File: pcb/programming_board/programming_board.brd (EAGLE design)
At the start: 100 x 80 mm, 28 parts, among them IC1 4053D, IC2 74ABT125PW

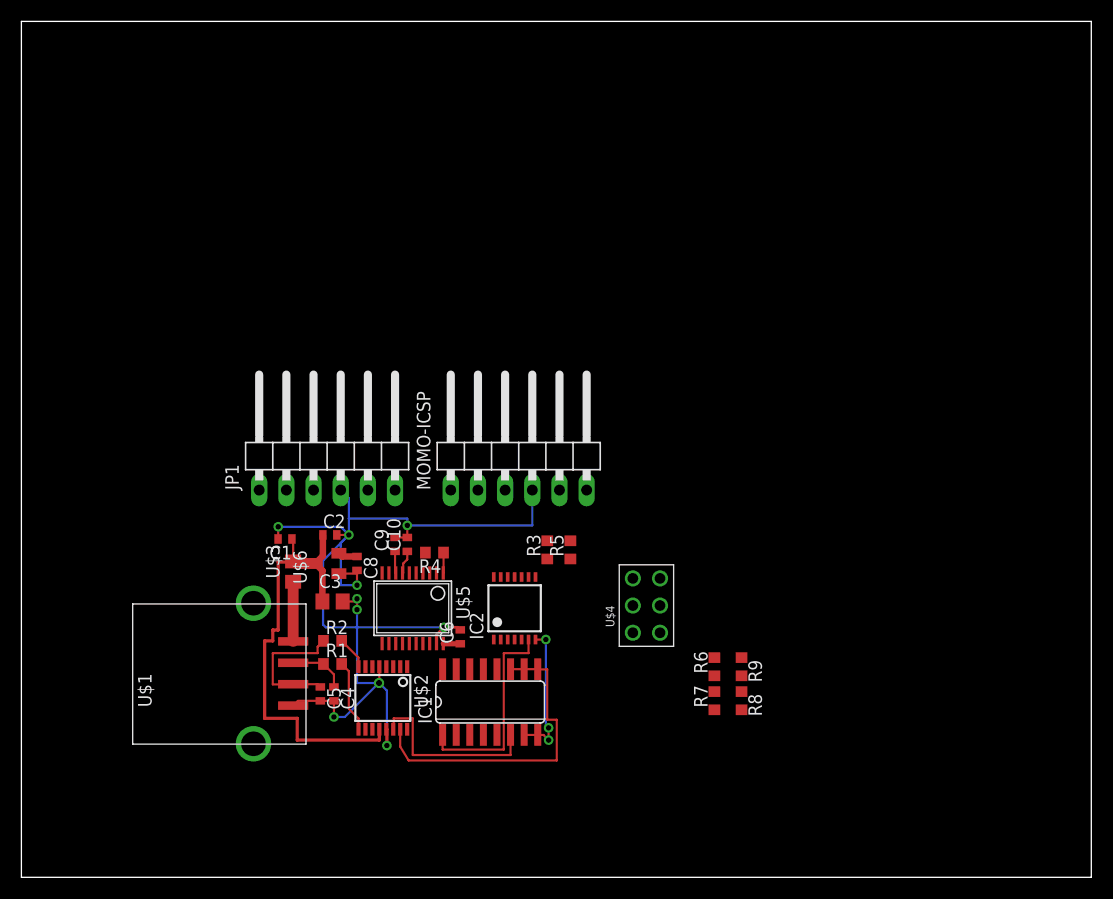
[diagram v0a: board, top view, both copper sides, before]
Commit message: Laid out first complete version of pcb
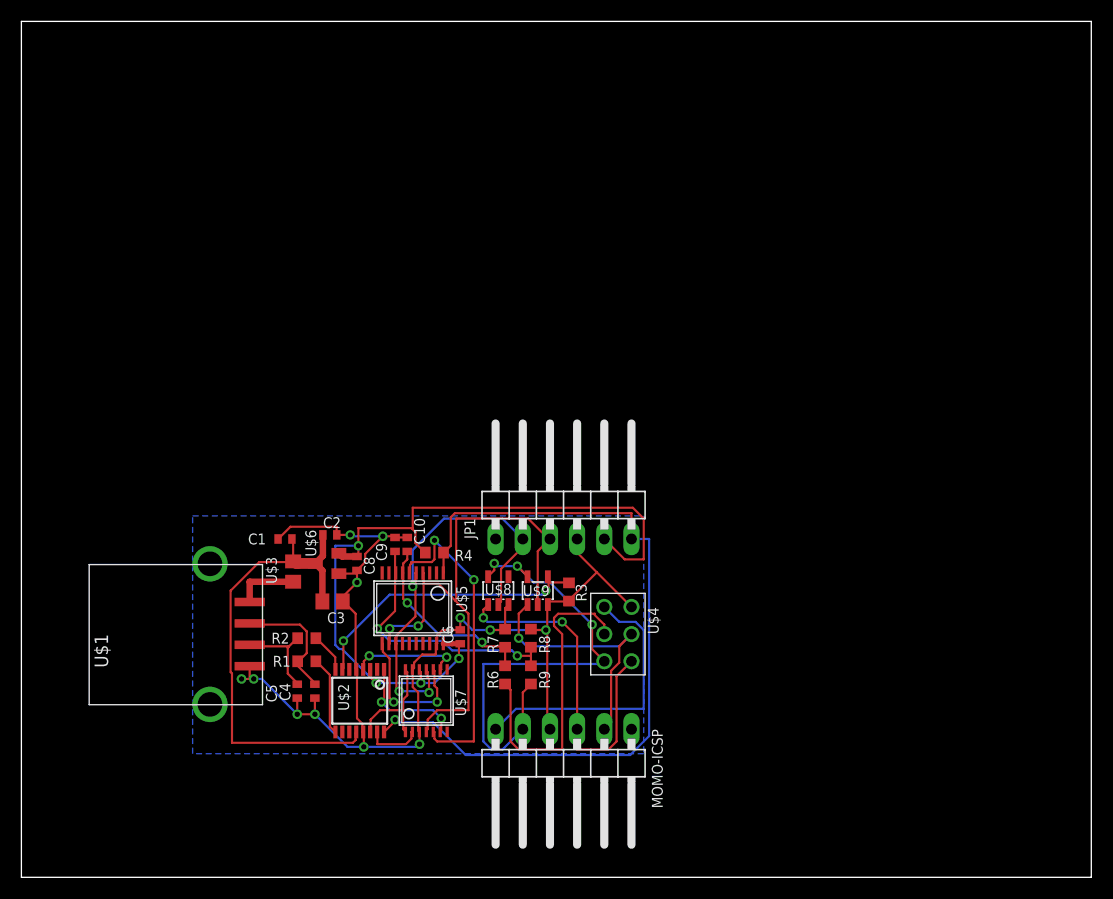
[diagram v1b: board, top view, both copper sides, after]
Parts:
- removed IC1: 4053D, 40xx:SO16
- removed IC2: 74ABT125PW, 74xx-us:TSSOP14
- removed R5: (no value), rcl:R0603
- added U$7: DG636, components:TSSOP14
- added U$8, U$9: TS5A1066-SPST, components:SOT23-5L
- R4: value (none) -> 10K
- moved MOMO-ICSP 30.3 mm to (50.7, 10.0), turned to 180 degrees
- moved JP1 22.6 mm to (50.7, 35.4)
- moved R8 20.5 mm to (47.6, 22.4)
- moved R7 20.4 mm to (45.2, 22.4), turned to 270 degrees
- moved R9 19.7 mm to (47.6, 18.9)
- moved R6 19.6 mm to (45.2, 18.9), turned to 270 degrees
- moved U$1 5.48 mm to (21.3, 22.7)
- moved R3 4.43 mm to (51.2, 26.7)
- moved U$4 2.67 mm to (57.0, 22.7), turned to 90 degrees
- moved R1 2.43 mm to (26.7, 20.2)
- moved R2 2.43 mm to (26.7, 22.4)
- moved C5 2.17 mm to (25.8, 17.4)
- moved U$2 2.17 mm to (31.6, 16.5)
- moved C4 1.80 mm to (27.4, 17.4)
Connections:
- removed net N$12: IC1.1, IC2.6
- removed net N$13: IC1.3, IC2.2
- removed net N$14: IC2.9, U$5.11
- removed net N$15: IC2.11, U$5.6
- removed net N$16: IC2.10, IC2.13, R5.1, U$5.13
- removed net N$18: IC1.5, JP1.2, U$5.5
- removed net N$19: IC1.2, JP1.3, U$5.4
- removed net N$8: IC1.15, U$2.4
- removed net N$9: IC1.10, IC1.11, IC1.9, U$2.15
- new net CLOCKRX: JP1.3, U$5.12, U$5.4, U$7.4, U$9.2
- new net DATATX: JP1.2, U$5.13, U$5.5, U$7.11, U$8.2
- new net PICRX1: U$5.6, U$7.5
- new net PICTX1: U$5.11, U$7.10
- new net USBRX: U$2.4, U$7.9
- new net USBTX: U$2.1, U$7.6
- net +3V3: now also U$8.5, U$9.5; no longer IC2.14, R3.2, R5.2
- net GND: now also R3.1, U$7.13, U$7.3, U$8.3, U$9.3; no longer IC1.7, IC1.8, IC2.7
- net N$10: now also U$2.15, U$7.2; no longer IC2.1, IC2.4, R3.1, U$2.7
- net N$11: now also U$7.1, U$7.14; no longer IC1.6
- net N$21: now also U$2.16
- net N$7: now also R3.2, U$2.7, U$9.4; no longer IC1.4, U$2.1
- net PGC: now also U$9.1; no longer IC2.3, IC2.8
- net PGD: now also U$8.1; no longer IC2.12, IC2.5
- net VCCIO: now also U$7.12; no longer IC1.16
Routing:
- net VCCIO: track 3.41 -> 76.0 mm, vias 0 -> 4
- net N$21: track 1.92 -> 72.5 mm, vias 0 -> 1
- net CLOCKRX: track 0.00 -> 53.1 mm, vias 0 -> 2
- net +3V3: track 0.00 -> 46.2 mm, vias 0 -> 3
- net DATATX: track 0.00 -> 40.2 mm, vias 0 -> 3
- net PGD: track 0.00 -> 33.5 mm, vias 0 -> 2
- net PICRX1: track 0.00 -> 30.0 mm, vias 0 -> 2
- net N$9: track 29.8 -> 0.00 mm
- net V+: track 0.00 -> 29.6 mm
- net N$7: track 0.00 -> 27.5 mm, vias 0 -> 2
- net N$6: track 0.00 -> 26.6 mm
- net PGC: track 0.00 -> 24.8 mm, vias 0 -> 1
- net N$20: track 2.08 -> 25.1 mm, vias 0 -> 2
- net N$12: track 19.7 -> 0.00 mm
- net N$17: track 2.24 -> 18.1 mm, vias 0 -> 2
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- added copper zone on layer 16, net GND

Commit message: Finished programming board (Momo Field Service Unit)
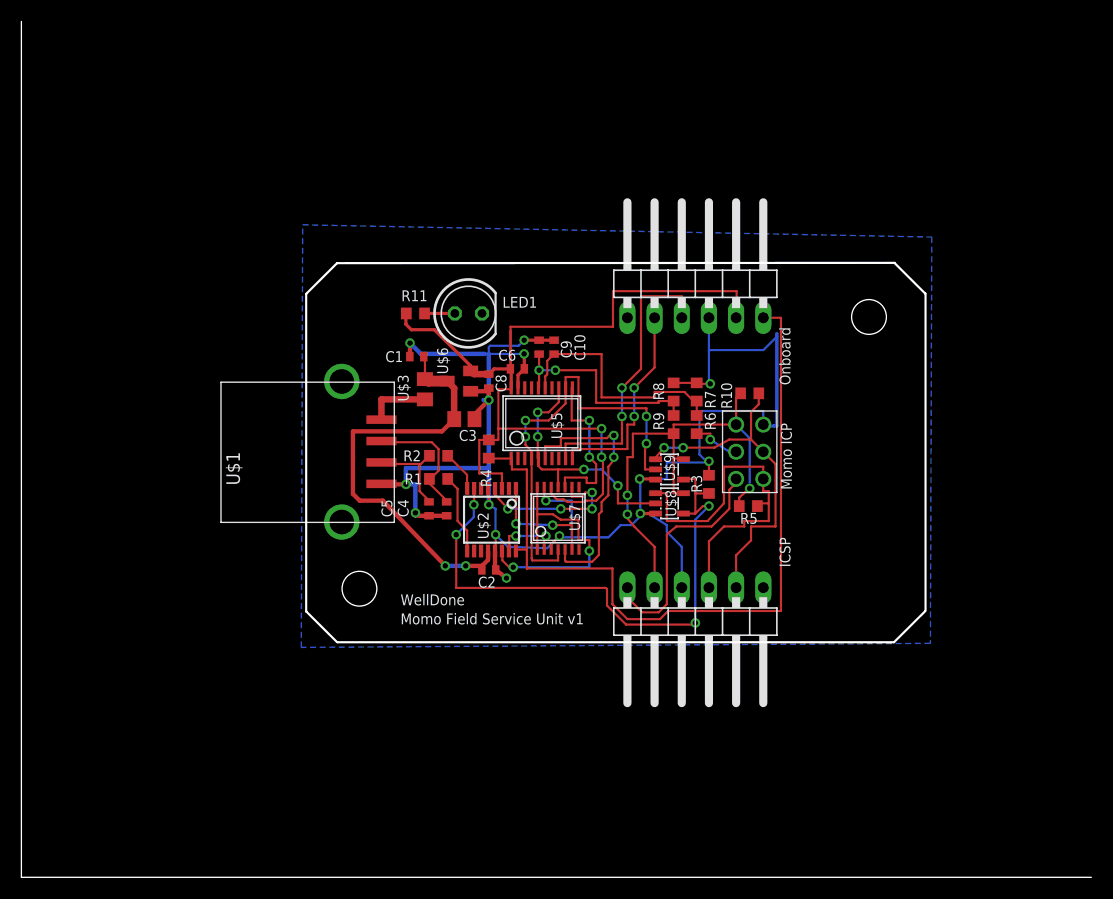
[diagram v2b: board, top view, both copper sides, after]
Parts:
- added LED1: (no value), led:LED5MM
- added R10: 10K, rcl:R0603
- added R11: 66R, rcl:R0603
- added R5: 19K, rcl:R0603
- moved R6 29.5 mm to (63.1, 42.3)
- moved R7 29.2 mm to (63.1, 45.4)
- moved R9 26.9 mm to (61.0, 42.3)
- moved R8 26.6 mm to (61.0, 45.4)
- moved C6 25.6 mm to (46.4, 47.5), turned to 0 degrees
- moved JP1 24.1 mm to (63.0, 56.1)
- moved C10 23.0 mm to (49.8, 49.6)
- moved C9 22.8 mm to (48.4, 49.6)
- moved U$5 21.1 mm to (48.6, 42.4), turned to 0 degrees
- moved C8 21.0 mm to (43.7, 46.4)
- moved U$1 21.0 mm to (33.7, 39.8)
- moved U$3 21.0 mm to (37.7, 45.6)
- moved U$7 21.0 mm to (50.2, 33.6)
- moved C1 21.0 mm to (37.0, 48.7)
- moved C3 21.0 mm to (41.4, 42.8)
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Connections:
- new net N$12: LED1.A, R11.1
- new net N$8: JP1.2, U$5.10
- new net N$9: JP1.3, U$5.9
- net +3V3: now also R10.2, R5.2, U$4.3; no longer U$4.1
- net CLOCKRX: no longer JP1.3
- net DATATX: no longer JP1.2
- net GND: now also LED1.K
- net N$17: now also U$5.15; no longer U$5.7
- net N$20: now also U$5.16; no longer U$5.8
- net N$6: now also U$4.1; no longer U$4.3
- net N$7: now also U$8.4
- net PGC: now also R10.1
- net PGD: now also R5.1
- net VCCIO: now also R11.2
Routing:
- net GND: track 116.9 -> 160.0 mm, vias 12 -> 15
- net N$7: track 27.5 -> 54.6 mm, vias 2 -> 4
- net N$9: track 0.00 -> 27.0 mm, vias 0 -> 2
- net V+: track 29.6 -> 4.57 mm, vias 0 -> 1
- net N$8: track 0.00 -> 19.7 mm, vias 0 -> 2
- net DATATX: track 40.2 -> 23.8 mm, vias 3 -> 4
- net N$11: track 10.7 -> 24.6 mm, vias 0 -> 2
- net CLOCKRX: track 53.1 -> 40.9 mm, vias 2 -> 4
- net PGC: track 24.8 -> 32.0 mm, vias 1 -> 2
- net VCCIO: track 76.0 -> 82.3 mm, vias 4 -> 2
- net PICRX1: track 30.0 -> 24.6 mm
- net N$17: track 18.1 -> 23.1 mm, vias 2 -> 0
- net N$20: track 25.1 -> 20.3 mm
- net N$6: track 26.6 -> 21.9 mm
- net USBRX: track 10.2 -> 14.8 mm, vias 2 -> 4
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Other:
- outline, holes or cut-outs redrawn
- board text added: "ICSP"
- board text added: "Momo Field Service Unit v1"
- board text added: "Momo ICP"
- board text added: "Onboard"
- board text added: "WellDone"

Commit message: Final version 1.0 of the programming board
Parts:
- added LED2: (no value), led:LED5MM
- added R12: 66R, rcl:R0603
- R5: value 19K -> 10K
- moved R10 10.8 mm to (78.9, 45.1)
- moved R5 10.8 mm to (78.7, 34.6)
- moved U$4 10.8 mm to (80.1, 39.6)
- moved C4 6.86 mm to (46.6, 34.3)
- moved C6 6.86 mm to (53.2, 47.4)
- moved R1 6.86 mm to (45.8, 37.1)
- moved R2 6.86 mm to (45.8, 39.3)
- moved R3 6.86 mm to (71.1, 36.6)
- moved R6 6.86 mm to (70.0, 42.2)
- moved R7 6.86 mm to (70.0, 45.2)
- moved U$6 6.86 mm to (47.8, 46.3)
- moved U$7 6.86 mm to (57.0, 33.4)
- moved C10 6.86 mm to (56.6, 49.4)
- moved U$5 6.86 mm to (55.5, 42.3)
- moved C1 6.86 mm to (43.8, 48.5)
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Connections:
- new net N$13: LED2.A, R12.1
- net +3V3: now also R12.2
- net GND: now also LED2.K
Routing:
- net PGD: track 34.6 -> 61.0 mm
- net PGC: track 32.0 -> 51.1 mm
- net GND: track 160.0 -> 177.7 mm
- net N$21: track 72.1 -> 82.0 mm
- net N$6: track 21.9 -> 28.5 mm
- net N$13: track 0.00 -> 6.06 mm
- net +3V3: track 45.6 -> 51.0 mm
- net V+: track 4.57 -> 8.28 mm
- net VCCIO: track 82.3 -> 79.2 mm
- net N$7: track 54.6 -> 53.7 mm
- net N$12: track 2.83 -> 3.72 mm
- net N$9: track 27.0 -> 26.3 mm
- net N$8: track 19.7 -> 19.2 mm
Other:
- board size 100 x 80 mm -> 57.9 x 35.5 mm
- board text added: "Device"
- board text added: "Power"
